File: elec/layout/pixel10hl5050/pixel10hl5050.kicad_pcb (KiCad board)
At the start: 2 copper layers, 2 parts

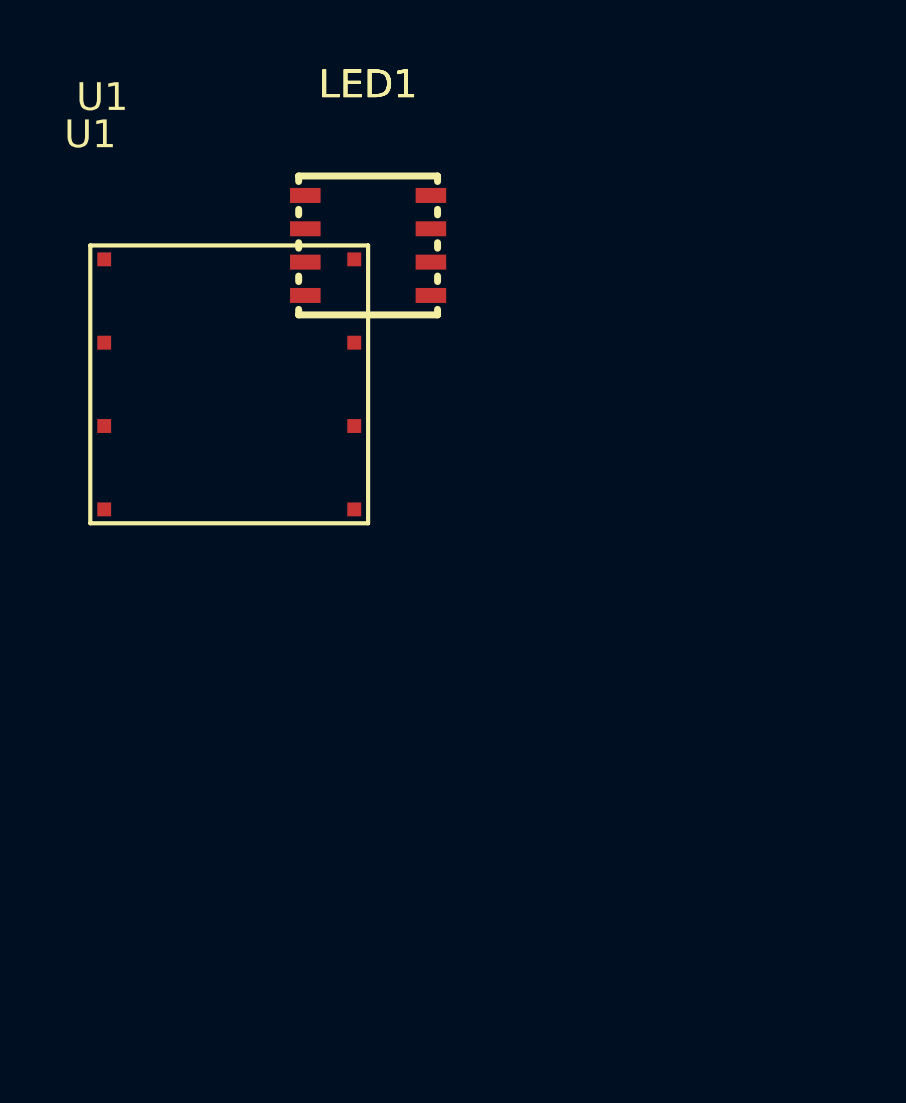
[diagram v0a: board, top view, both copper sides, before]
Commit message: pixel10hl5050 routing
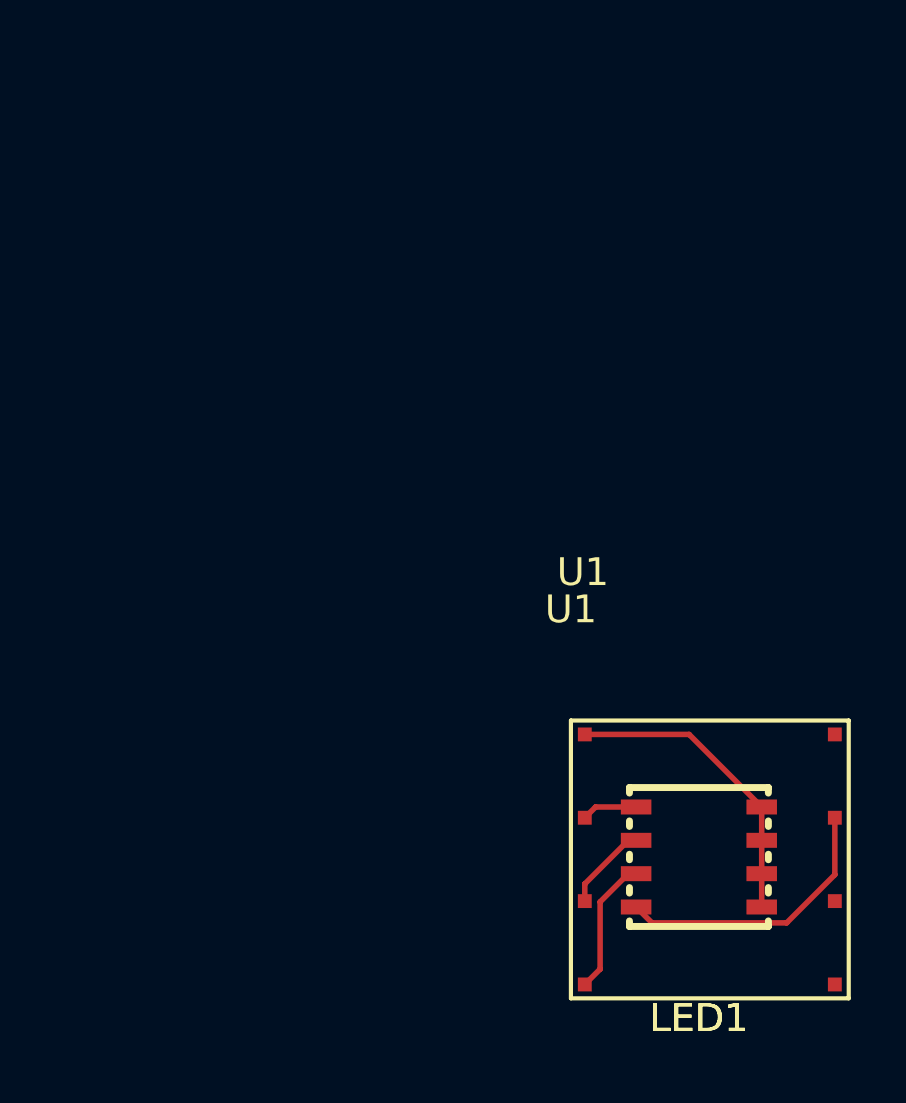
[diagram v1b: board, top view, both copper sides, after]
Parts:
- moved LED1 25.0 mm to (21.9, 22.0), turned to 180 degrees
- moved U1 24.3 mm to (17.3, 17.1)
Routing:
- net anode: track 0.00 -> 11.0 mm
- net cathode_cold_white: track 0.00 -> 10.2 mm
- net cathode_blue: track 0.00 -> 4.92 mm
- net cathode_green: track 0.00 -> 3.12 mm
- net cathode_red: track 0.00 -> 2.01 mm

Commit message: pixel refactor
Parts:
- moved U1 24.3 mm to (0.00, 0.00)
- moved LED1 24.0 mm to (5.01, 4.92), turned to 0 degrees
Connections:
- net cathode_blue renamed blue
- net cathode_cold_white renamed cold_white
- net cathode_green renamed green
- net cathode_ir renamed ir
- net cathode_red renamed red
- net cathode_uv renamed uv
- net cathode_warm_white renamed warm_white
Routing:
- net anode: track 11.0 -> 0.00 mm
- net cold_white: track 10.2 -> 0.00 mm
- net blue: track 4.92 -> 0.00 mm
- net green: track 3.12 -> 0.00 mm
- net red: track 2.01 -> 0.00 mm

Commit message: updating rp2040
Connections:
- LED1 pad 1: cold_white -> rgb-cathodes-cathode-1
- LED1 pad 3: blue -> rgb-cathodes-cathode-0
- LED1 pad 5: green -> rgb-cathodes-cathode-2
- LED1 pad 7: red -> rgb-cathodes-cathode-3
